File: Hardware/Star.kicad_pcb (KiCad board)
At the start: 2 copper layers, 82.6 x 94.1 mm, 114 parts, among them P1 JTAGICE3, P2 UART, P3 USB_OTG, P4 SPI_FLASH, Q1 BSS806NE, Q10 BSS806NE, Q11 BSS806NE, Q12 BSS806NE, Q13 BSS806NE, Q2 BSS806NE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

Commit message: stuff
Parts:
- moved C2 1.02 mm to (110.5, 102.1)
- moved TVS1 0.09 mm to (102.8, 98.9)
- turned R24 to 0 degrees
- turned R25 to 0 degrees
- turned R31 to 90 degrees
- turned R32 to 90 degrees
- turned R41 to 180 degrees
- turned R42 to 180 degrees
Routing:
- net +3V: track 41.0 -> 311.7 mm, vias 0 -> 12
- net GND: track 74.1 -> 211.5 mm, vias 4 -> 12
- net Net-(D1-Pad4): track 0.00 -> 60.9 mm, vias 0 -> 5
- net Net-(D1-Pad3): track 0.00 -> 53.3 mm, vias 0 -> 3
- net /AOUT: track 0.00 -> 36.1 mm, vias 0 -> 2
- net /VREF: track 1.92 -> 31.0 mm
- net /FLASH_~WP: track 0.00 -> 20.3 mm, vias 0 -> 3
- net /USBD+: track 0.00 -> 19.4 mm
- net /USBD-: track 0.00 -> 18.4 mm
- net /FLASH_MOSI: track 0.00 -> 16.9 mm, vias 0 -> 2
- net /FLASH_~CS: track 2.33 -> 19.2 mm, vias 0 -> 3
- net /FLASH_SCK: track 0.00 -> 16.5 mm, vias 0 -> 3
- net Net-(D3-Pad2): track 0.00 -> 15.2 mm, vias 0 -> 1
- net Net-(D3-Pad3): track 0.00 -> 14.9 mm, vias 0 -> 1
- net Net-(D3-Pad4): track 0.00 -> 11.4 mm, vias 0 -> 3
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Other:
- net class Default: clearance 0 -> 0.1524
- rule pad_to_mask_clearance: 0.1016 -> 0.0762
- rule trace_clearance: 0 -> 0.1524

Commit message: Finished routing
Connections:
- C18 pad 1: /~PB -> ~PB
- R28 pad 2: /~PB -> ~PB
- SW2 pad 2: /~PB -> ~PB
- U3 pad 11: GLED_6 -> GLED_2
- U3 pad 12: RLED_6 -> RLED_2
- U3 pad 13: /~PB -> Net-(U3-Pad13)
- U3 pad 15: GLED_5 -> GLED_1
- U3 pad 16: RLED_5 -> RLED_1
- U3 pad 17: GLED_4 -> GLED_3
- U3 pad 18: RLED_4 -> RLED_3
- U3 pad 19: GLED_3 -> GLED_4
- U3 pad 20: RLED_3 -> RLED_4
- U3 pad 23: GLED_2 -> GLED_6
- U3 pad 24: RLED_2 -> RLED_6
- U3 pad 25: GLED_1 -> GLED_5
- U3 pad 26: RLED_1 -> RLED_5
- U3 pad 51: Net-(U3-Pad51) -> ~PB
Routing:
- net +3V: track 311.7 -> 505.6 mm, vias 12 -> 21
- net GND: track 211.5 -> 324.3 mm, vias 12 -> 50
- net GLED_5: track 1.62 -> 97.1 mm, vias 1 -> 12
- net RLED_5: track 0.99 -> 92.3 mm, vias 1 -> 12
- net ~PB: track 0.00 -> 89.6 mm, vias 0 -> 15
- net RLED_4: track 1.12 -> 79.5 mm, vias 1 -> 6
- net GLED_4: track 1.84 -> 77.6 mm, vias 1 -> 6
- net GLED_3: track 1.93 -> 75.9 mm, vias 1 -> 6
- net RLED_3: track 1.12 -> 71.3 mm, vias 1 -> 6
- net ~RST: track 7.11 -> 71.1 mm, vias 1 -> 10
- net GLED_6: track 1.01 -> 64.2 mm, vias 1 -> 6
- net RLED_6: track 1.61 -> 62.8 mm, vias 1 -> 6
- net SWDIO: track 1.82 -> 59.9 mm, vias 1 -> 12
- net SWDCLK: track 1.12 -> 59.0 mm, vias 1 -> 10
- net /UART_RX: track 1.19 -> 58.3 mm, vias 1 -> 4
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- added copper zone on B.Cu, net GND

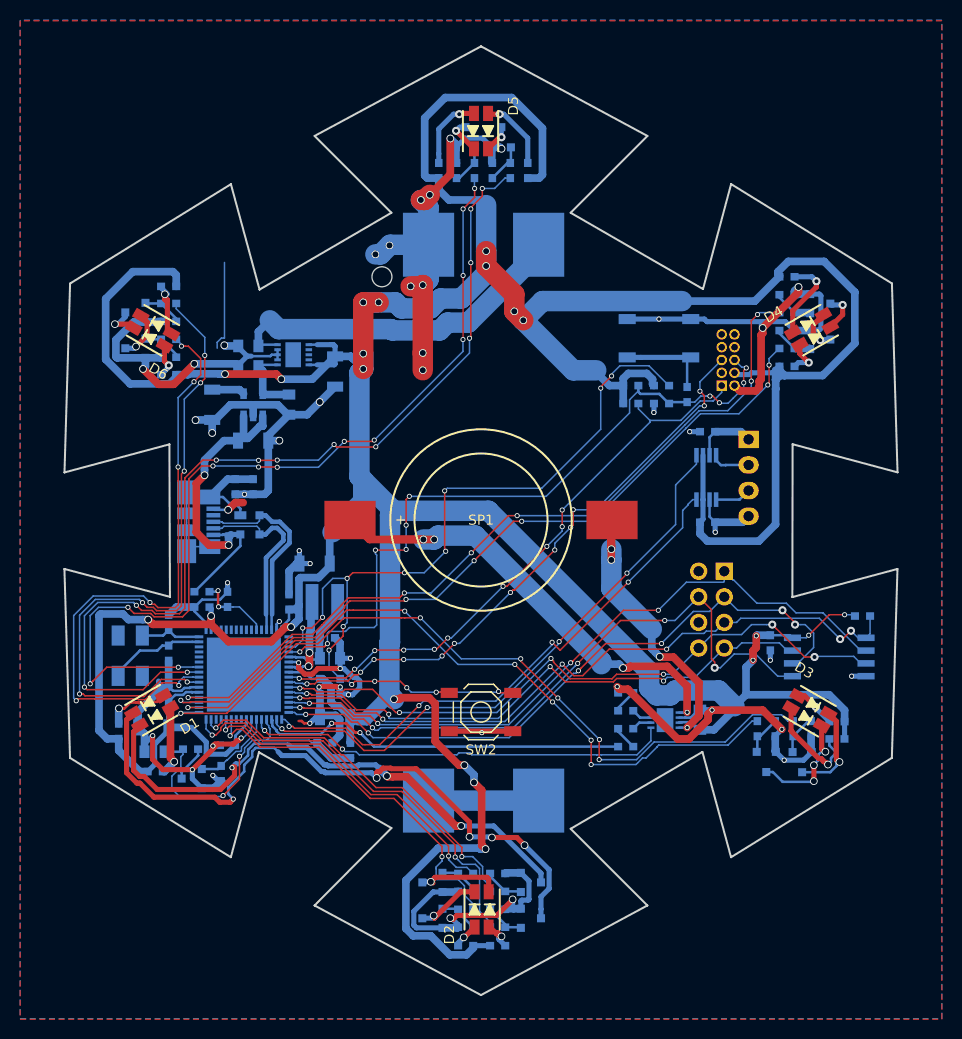
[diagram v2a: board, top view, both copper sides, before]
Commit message: Cleaned up gnd pours
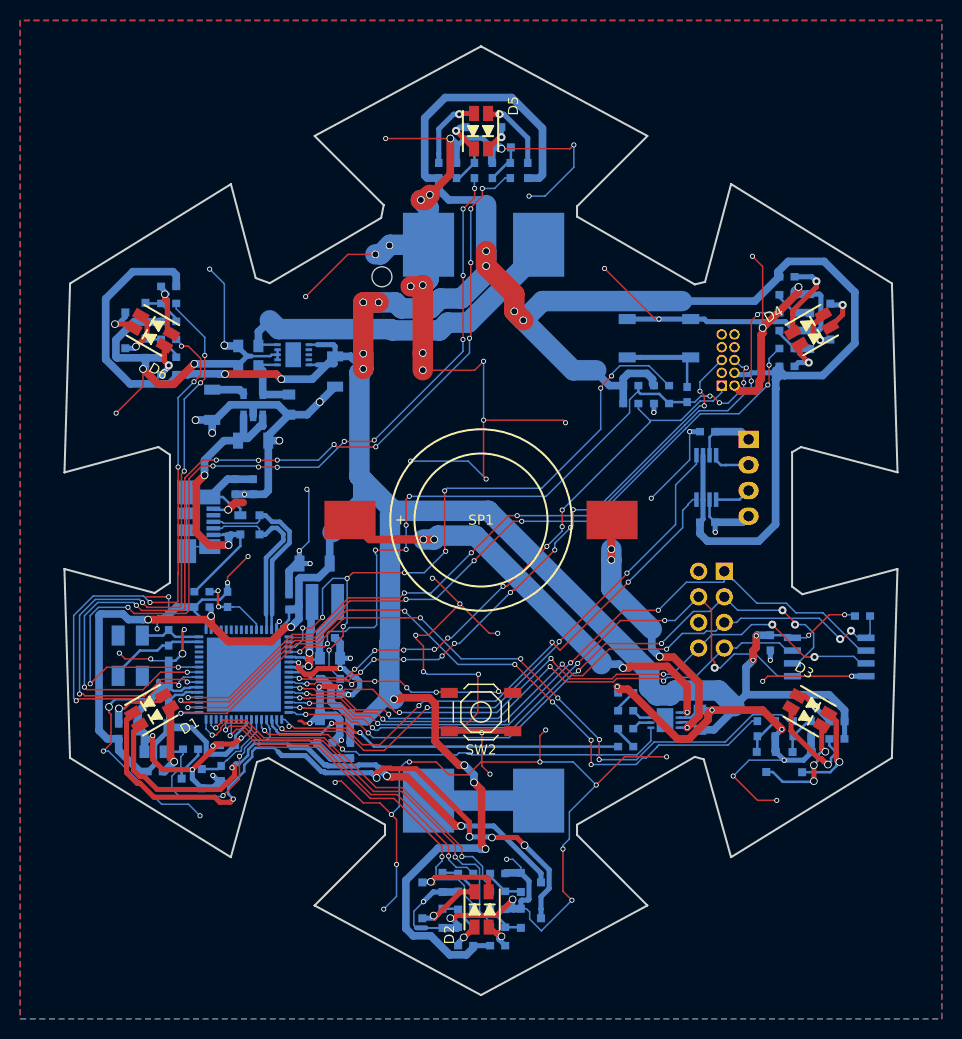
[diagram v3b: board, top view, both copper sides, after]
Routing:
- net GND: track 324.3 -> 613.8 mm, vias 50 -> 99
- net (no net): track 8.99 -> 0.00 mm
- net RLED_6: track 62.8 -> 62.3 mm
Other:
- outline, holes or cut-outs redrawn

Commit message: Silkscreened board
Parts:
- added REF**: MountingHole_2.2mm_M2_ISO7380, Mounting_Holes:MountingHole_2.2mm_M2_ISO7380, F.Cu at (127.0, 54.7)
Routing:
- net +3V: track 505.6 -> 483.7 mm
- net Net-(D1-Pad3): track 55.5 -> 54.0 mm
- net GND: track 613.8 -> 614.6 mm
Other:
- board text added: "2016"
- board text added: "John"
- board text added: "Merry Christmas"

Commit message: Finished hardware design
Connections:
- U2 pad 11: (no net) -> GND
- U5 pad 4: (no net) -> GND
- U5 pad 9: (no net) -> GND
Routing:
- net GND: track 614.6 -> 621.2 mm, vias 99 -> 103
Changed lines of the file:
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@@
 (kicad_pcb (version 20160815) (host pcbnew "(2016-12-02 revision 54c5f6b)-makepkg")
   (general
-    (links 0)
+    (links 266)
     (no_connects 0)
     (area 85.57102 50.699999 168.419059 145.018961)
     (thickness 1.6)
     (drawings 47)
-    (tracks 2355)
+    (tracks 2374)
     (zones 0)
     (modules 115)
@@
   )
   (setup
-    (last_trace_width 0.762)
+    (last_trace_width 0.25)
     (user_trace_width 0.1524)
     (user_trace_width 0.254)
@@
     (pad_drill 0.762)
     (pad_to_mask_clearance 0.0762)
+    (pad_to_paste_clearance_ratio -0.15)
     (aux_axis_origin 0 0)
     (visible_elements 7FFFFFFF)
@@
       (psa4output false)
       (plotreference true)
-      (plotvalue true)
+      (plotvalue false)
       (plotinvisibletext false)
       (padsonsilk false)
       (subtractmaskfromsilk false)
-      (outputformat 1)
+      (outputformat 4)
       (mirror false)
       (drillshape 0)
@@
       (net 115 +3V))
     (pad 11 smd rect (at 0.3875 -0.62) (size 0.775 1.24) (layers B.Cu B.Paste B.Mask)
-      (solder_paste_margin_ratio -0.2))
+      (net 1 GND) (solder_paste_margin_ratio -0.2))
     (pad 11 smd rect (at 0.3875 0.62) (size 0.775 1.24) (layers B.Cu B.Paste B.Mask)
-      (solder_paste_margin_ratio -0.2))
+      (net 1 GND) (solder_paste_margin_ratio -0.2))
     (pad 11 smd rect (at -0.3875 -0.62) (size 0.775 1.24) (layers B.Cu B.Paste B.Mask)
-      (solder_paste_margin_ratio -0.2))
+      (net 1 GND) (solder_paste_margin_ratio -0.2))
     (pad 11 smd rect (at -0.3875 0.62) (size 0.775 1.24) (layers B.Cu B.Paste B.Mask)
-      (solder_paste_margin_ratio -0.2))
+      (net 1 GND) (solder_paste_margin_ratio -0.2))
     (model Housings_DFN_QFN.3dshapes/DFN-10-1EP_3x3mm_Pitch0.5mm.wrl
       (at (xyz 0 0 0))
@@
     (pad 3 smd rect (at -1.4 -0.25) (size 0.7 0.25) (layers B.Cu B.Paste B.Mask)
       (net 107 "Net-(R36-Pad2)"))
-    (pad 4 smd rect (at -1.4 -0.75) (size 0.7 0.25) (layers B.Cu B.Paste B.Mask))
+    (pad 4 smd rect (at -1.4 -0.75) (size 0.7 0.25) (layers B.Cu B.Paste B.Mask)
+      (net 1 GND))
     (pad 5 smd rect (at 1.4 -0.75) (size 0.7 0.25) (layers B.Cu B.Paste B.Mask)
       (net 113 /SPKR+))
@@
       (net 114 /SPKR-))
     (pad 9 smd rect (at 0.415 -0.595) (size 0.83 1.19) (layers B.Cu B.Paste B.Mask)
-      (solder_paste_margin_ratio -0.2))
+      (net 1 GND) (solder_paste_margin_ratio -0.2))
     (pad 9 smd rect (at 0.415 0.595) (size 0.83 1.19) (layers B.Cu B.Paste B.Mask)
-      (solder_paste_margin_ratio -0.2))
+      (net 1 GND) (solder_paste_margin_ratio -0.2))
     (pad 9 smd rect (at -0.415 -0.595) (size 0.83 1.19) (layers B.Cu B.Paste B.Mask)
-      (solder_paste_margin_ratio -0.2))
+      (net 1 GND) (solder_paste_margin_ratio -0.2))
     (pad 9 smd rect (at -0.415 0.595) (size 0.83 1.19) (layers B.Cu B.Paste B.Mask)
-      (solder_paste_margin_ratio -0.2))
+      (net 1 GND) (solder_paste_margin_ratio -0.2))
     (model Housings_DFN_QFN.3dshapes/DFN-8-1EP_3x3mm_Pitch0.5mm.wrl
       (at (xyz 0 0 0))
@@
   (segment (start 121.412 63.609) (end 121.176 63.609) (width 0.762) (layer F.Cu) (net 0))
   (segment (start 121.176 63.609) (end 121.031 63.754) (width 0.762) (layer F.Cu) (net 0))
+  (segment (start 108.753021 82.015361) (end 108.753021 82.445479) (width 0.25) (layer B.Cu) (net 1))
+  (segment (start 108.753021 82.445479) (end 108.204 82.9945) (width 0.25) (layer B.Cu) (net 1))
+  (via (at 108.204 82.9945) (size 0.508) (drill 0.3302) (layers F.Cu B.Cu) (net 1))
+  (segment (start 105.791 81.534) (end 104.2035 81.534) (width 0.254) (layer B.Cu) (net 1))
+  (segment (start 106.815521 81.395361) (end 105.929639 81.395361) (width 0.25) (layer B.Cu) (net 1))
+  (segment (start 105.929639 81.395361) (end 105.791 81.534) (width 0.25) (layer B.Cu) (net 1))
+  (via (at 105.791 81.534) (size 0.508) (drill 0.3302) (layers F.Cu B.Cu) (net 1))
+  (segment (start 106.815521 80.895361) (end 106.815521 81.2165) (width 0.254) (layer B.Cu) (net 1))
+  (segment (start 106.815521 81.2165) (end 106.815521 81.395361) (width 0.254) (layer B.Cu) (net 1))
+  (segment (start 107.978021 80.775361) (end 107.340521 80.775361) (width 0.25) (layer B.Cu) (net 1))
+  (segment (start 107.340521 80.775361) (end 106.899382 81.2165) (width 0.25) (layer B.Cu) (net 1))
+  (segment (start 106.899382 81.2165) (end 106.815521 81.2165) (width 0.25) (layer B.Cu) (net 1))
+  (segment (start 145.669 118.237) (end 145.669 118.8085) (width 0.25) (layer B.Cu) (net 1))
+  (segment (start 145.669 118.8085) (end 145.2245 119.253) (width 0.25) (layer B.Cu) (net 1))
+  (via (at 145.2245 119.253) (size 0.508) (drill 0.3302) (layers F.Cu B.Cu) (net 1))
+  (segment (start 141.56692 114.57942) (end 143.383 116.3955) (width 0.762) (layer F.Cu) (net 1))
+  (segment (start 143.383 116.3955) (end 146.4945 119.507) (width 0.762) (layer F.Cu) (net 1))
+  (segment (start 143.854 116.892) (end 143.854 116.8665) (width 0.25) (layer B.Cu) (net 1))
+  (segment (start 143.854 116.8665) (end 143.383 116.3955) (width 0.25) (layer B.Cu) (net 1))
+  (via (at 143.383 116.3955) (size 0.508) (drill 0.3302) (layers F.Cu B.Cu) (net 1))
+  (segment (start 143.854 116.892) (end 144.684 116.892) (width 0.25) (layer B.Cu) (net 1))
+  (segment (start 144.684 116.892) (end 144.839 117.047) (width 0.25) (layer B.Cu) (net 1))
+  (segment (start 146.654 117.392) (end 146.014 117.392) (width 0.25) (layer B.Cu) (net 1))
+  (segment (start 146.014 117.392) (end 145.669 117.047) (width 0.25) (layer B.Cu) (net 1))
   (segment (start 90.0938 116.332) (end 90.0938 116.7765) (width 0.1524) (layer F.Cu) (net 1))
   (segment (start 90.0938 116.7765) (end 90.0938 116.870815) (width 0.1524) (layer F.Cu) (net 1))
@@
   (segment (start 149.529809 117.599761) (end 149.529809 117.043191) (width 0.762) (layer F.Cu) (net 1))
   (segment (start 149.529809 117.043191) (end 149.9235 116.6495) (width 0.762) (layer F.Cu) (net 1))
-  (segment (start 141.56692 114.57942) (end 146.4945 119.507) (width 0.762) (layer F.Cu) (net 1))
   (segment (start 140.508459 114.325421) (end 140.762458 114.57942) (width 0.762) (layer F.Cu) (net 1))
   (segment (start 140.762458 114.57942) (end 141.56692 114.57942) (width 0.762) (layer F.Cu) (net 1))
@@
   (segment (start 93.615 120.777) (end 93.615 118.991) (width 0.762) (layer B.Cu) (net 1))
   (segment (start 93.615 118.991) (end 92.988 118.364) (width 0.762) (layer B.Cu) (net 1))
-  (segment (start 106.097882 81.534) (end 104.2035 81.534) (width 0.254) (layer B.Cu) (net 1))
   (segment (start 103.80166 81.534) (end 104.2035 81.534) (width 0.508) (layer B.Cu) (net 1))
   (segment (start 102.914021 82.553361) (end 102.914021 82.421639) (width 0.508) (layer B.Cu) (net 1))
@@
   (segment (start 105.894 94.875) (end 105.531 95.238) (width 0.762) (layer B.Cu) (net 1))
   (segment (start 105.531 95.238) (end 104.394 95.238) (width 0.762) (layer B.Cu) (net 1))
-  (segment (start 106.815521 81.395361) (end 106.236521 81.395361) (width 0.254) (layer B.Cu) (net 1))
-  (segment (start 106.236521 81.395361) (end 106.097882 81.534) (width 0.254) (layer B.Cu) (net 1))
   (segment (start 106.815521 81.395361) (end 106.815521 81.895361) (width 0.254) (layer B.Cu) (net 1))
-  (segment (start 106.815521 80.895361) (end 106.815521 81.395361) (width 0.254) (layer B.Cu) (net 1))
   (segment (start 107.95 87.344) (end 109.736 87.344) (width 0.762) (layer B.Cu) (net 1))
   (segment (start 102.13 86.36) (end 104.267 86.36) (width 0.762) (layer B.Cu) (net 1))
